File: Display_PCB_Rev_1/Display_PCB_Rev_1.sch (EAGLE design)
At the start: 5 parts, among them J1 71430-015

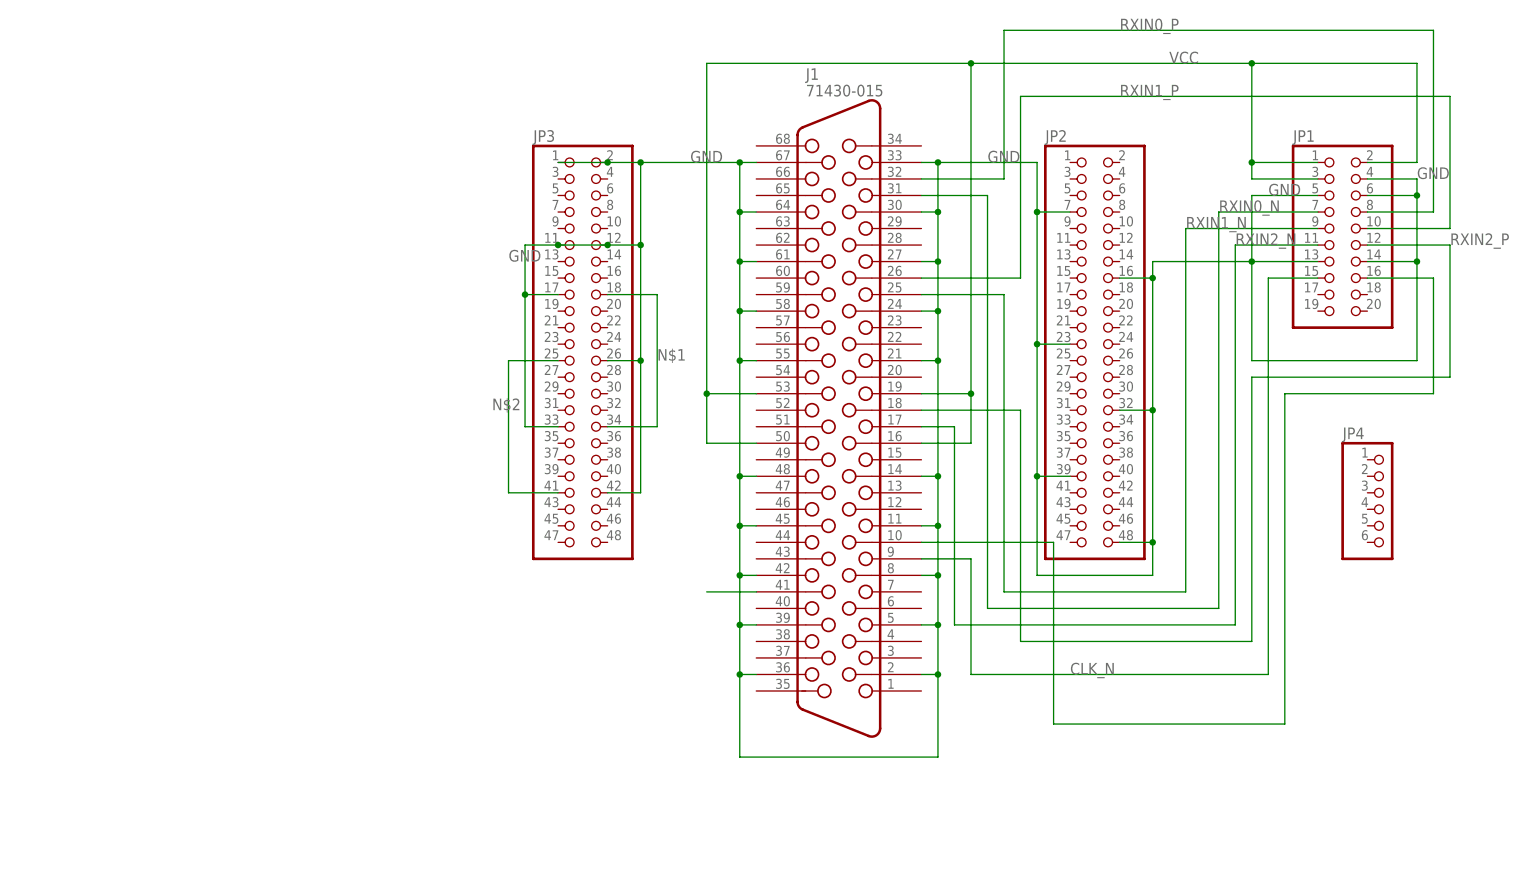
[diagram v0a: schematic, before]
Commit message: Cleaned up schematic and layout; Added DC Barrel Jack and coupling capacitor; filtering circuit for shield
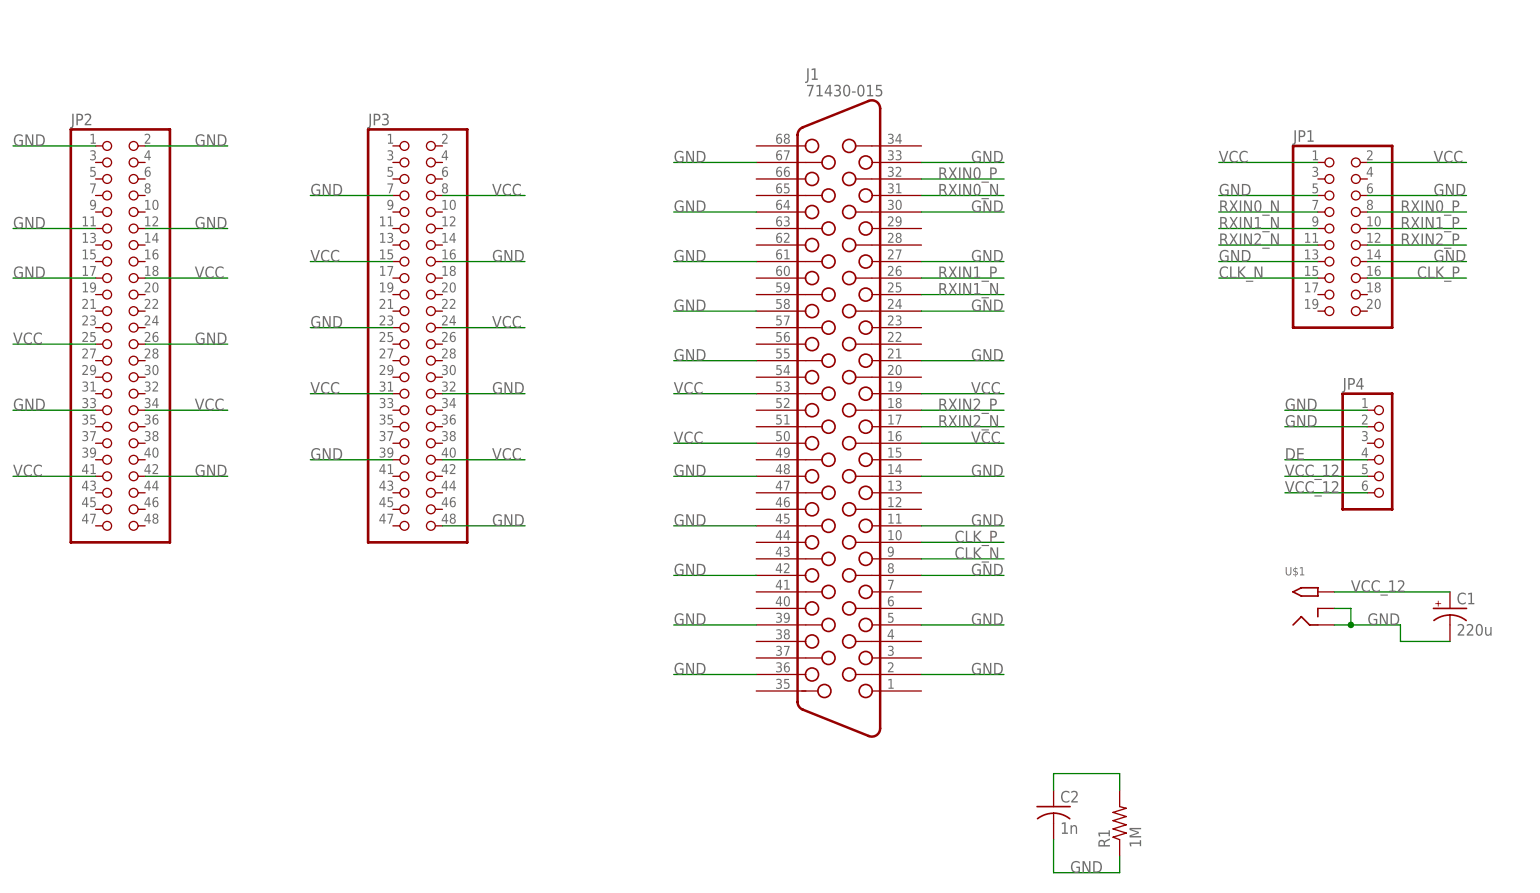
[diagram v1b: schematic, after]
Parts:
- added C1: 220u, resistor:CPOL-USE5-8.5
- added C2: 1n, resistor:C-USC0805
- added R1: 1M, resistor:R-US_R0805W
- added U$1: 2.1MMJACKTHM, adafruit:2.1MMJACKTHM
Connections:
- removed net N$2: JP3.25, JP3.41
- removed net N$4: J1.41
- new net DE: JP4.4
- new net VCC_12: C1.+, JP4.5, JP4.6, U$1.TIP
- net GND: now also C1.-, C2.2, JP2.1, JP2.11, JP2.12, JP2.17, JP2.2, JP2.26, JP2.33, JP2.42, JP3.16, JP3.23, JP3.32, JP3.39, JP3.48, JP3.7, JP4.1, JP4.2, R1.1, U$1.RING, U$1.RING_SW; no longer JP1.4, JP2.16, JP2.23, JP2.32, JP2.39, JP2.48, JP2.7, JP3.1, JP3.11, JP3.12, JP3.17, JP3.2, JP3.26, JP3.33, JP3.42
- net N$1: now also C2.1, R1.2; no longer JP3.18, JP3.34
- net VCC: now also J1.19, JP2.18, JP2.25, JP2.34, JP2.41, JP3.15, JP3.24, JP3.31, JP3.40, JP3.8; no longer JP1.3
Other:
- moved on the sheet: JP2, JP3, JP4

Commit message: first set of differential pairs
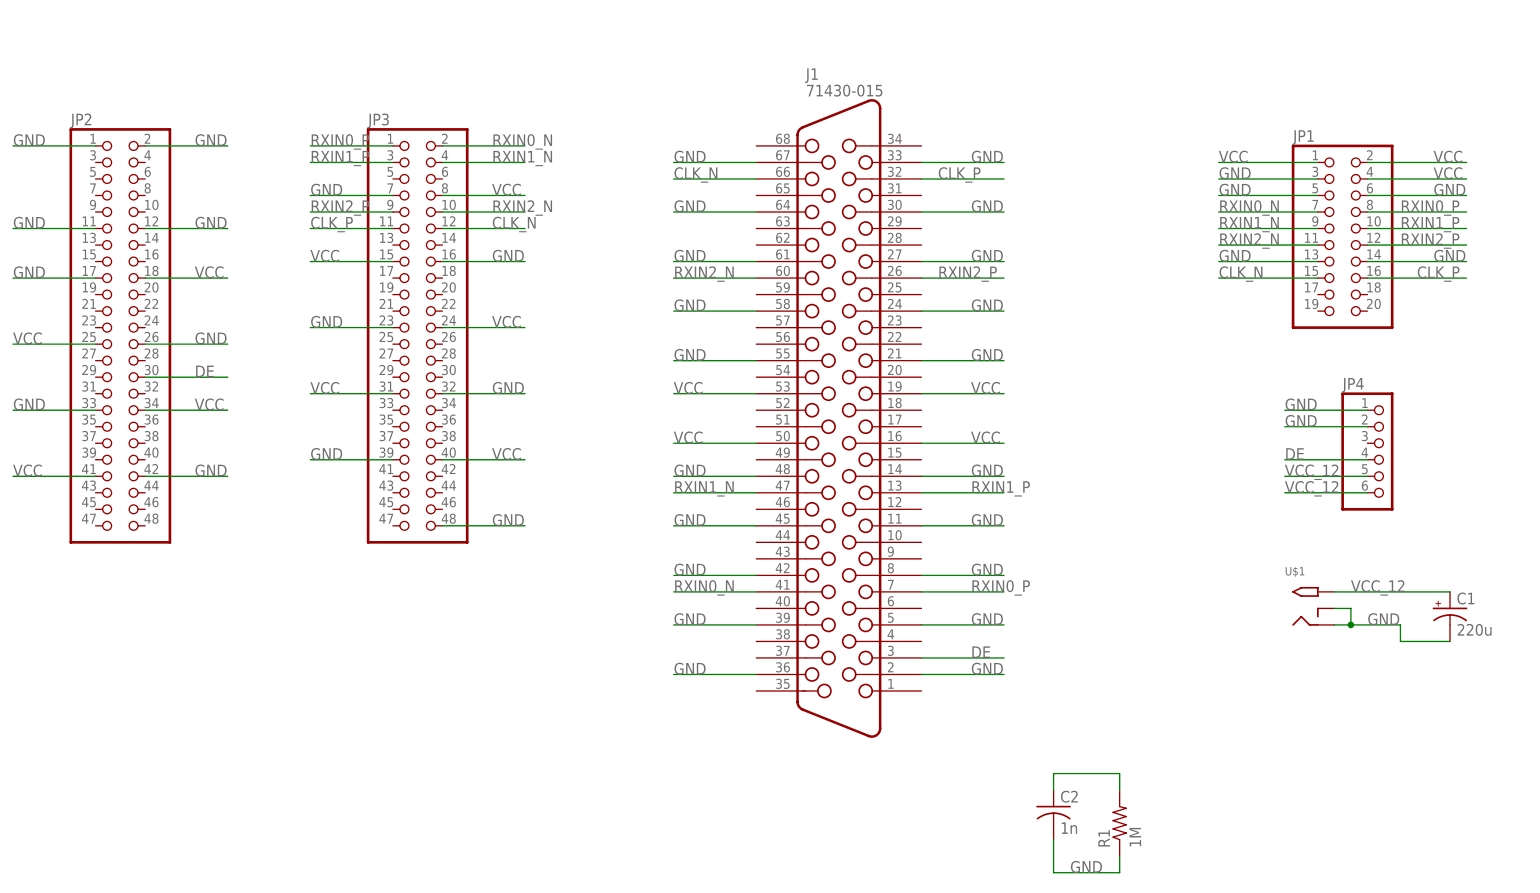
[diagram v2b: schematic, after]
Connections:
- net CLK_N: now also J1.66, JP3.12; no longer J1.9
- net CLK_P: now also J1.32, JP3.11; no longer J1.10
- net DE: now also J1.3, JP2.30
- net GND: now also JP1.3
- net RXIN0_N: now also J1.41, JP3.2; no longer J1.31
- net RXIN0_P: now also J1.7, JP3.1; no longer J1.32
- net RXIN1_N: now also J1.47, JP3.4; no longer J1.25
- net RXIN1_P: now also J1.13, JP3.3; no longer J1.26
- net RXIN2_N: now also J1.60, JP3.10; no longer J1.17
- net RXIN2_P: now also J1.26, JP3.9; no longer J1.18
- net VCC: now also JP1.4
